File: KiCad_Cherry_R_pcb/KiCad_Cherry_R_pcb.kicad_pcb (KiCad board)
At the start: 2 copper layers, 188.7 x 100 mm, 89 parts, among them J1 AudioJack3_SwitchTR, SW1 7, SW10 I, SW11 O, SW12 P, SW13 [, SW14 ], SW15 H, SW16 J, SW17 K, SW18 L, SW19 ;, SW2 8, SW20 ', SW21 \, SW22 B, SW23 N, SW24 M, SW25 ,, SW26 ., SW27 /, SW28 Shift, SW29 Space, SW3 9, SW30 Conv, SW31 Win, SW32 Fn, SW33 ←, SW34 ↑, SW35 ↓, SW36 BS, SW37 Enter, SW38 Home, SW39 End, SW4 0, SW40 →, SW41 Free, SW42 PrtSc, SW5 -, SW6 =, SW7 `, SW8 Y, SW9 U, U1 Sparkfun_Pro_Micro

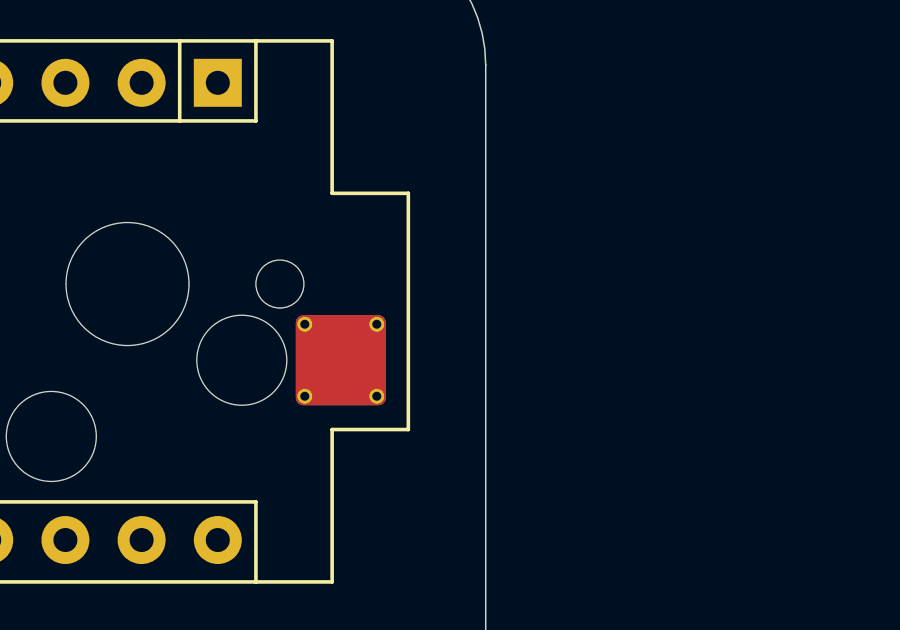
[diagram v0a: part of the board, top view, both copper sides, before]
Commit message: feat: Resetピンを追加
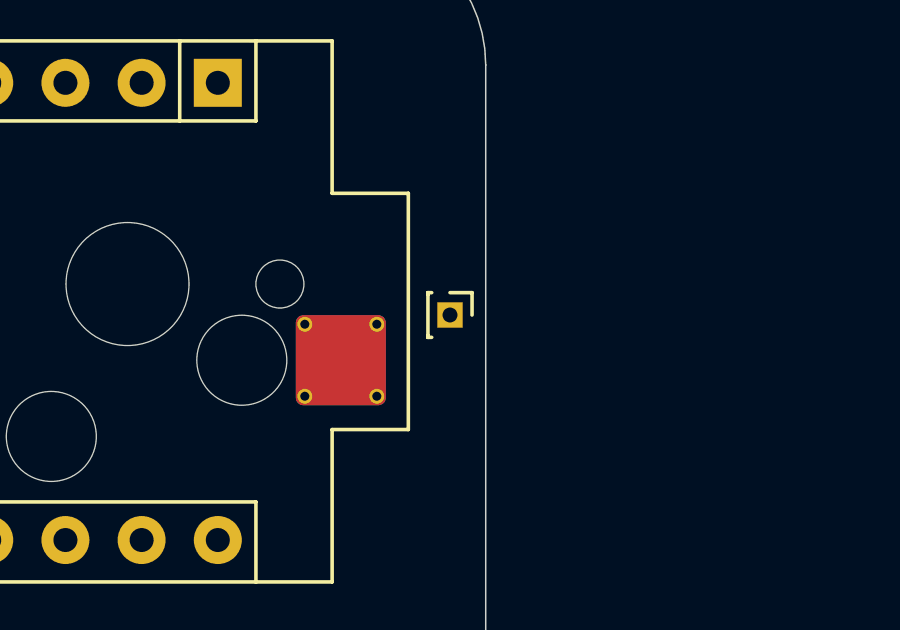
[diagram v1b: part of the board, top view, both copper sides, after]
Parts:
- added J2: Reset, Connector_PinHeader_1.00mm:PinHeader_1x01_P1.00mm_Vertical, F.Cu at (220.3, 48.8)
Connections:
- U1 pad 22: unconnected-(U1-RST-Pad22) -> Net-(J2-Pin_1)
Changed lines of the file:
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@@
 	(net 47 "Col5")
 	(net 48 "unconnected-(U1-RAW-Pad24)")
-	(net 49 "unconnected-(U1-RST-Pad22)")
+	(net 49 "Net-(J2-Pin_1)")
 	(net 50 "Net-(D33-A)")
 	(net 51 "unconnected-(U1-D0{slash}RX-Pad2)")
@@
 			(layers "*.Cu" "*.Mask")
 			(remove_unused_layers no)
-			(net 49 "unconnected-(U1-RST-Pad22)")
+			(net 49 "Net-(J2-Pin_1)")
 			(pinfunction "RST")
-			(pintype "input+no_connect")
+			(pintype "input")
 		)
 		(pad "23" thru_hole oval
@@
 			)
 			(scale
+				(xyz 1 1 1)
+			)
+			(rotate
+				(xyz 0 0 0)
+			)
+		)
+	)
+	(footprint "Connector_PinHeader_1.00mm:PinHeader_1x01_P1.00mm_Vertical"
+		(layer "F.Cu")
+		(at 220.26581 48.815666 -90)
+		(descr "Through hole straight pin header, 1x01, 1.00mm pitch, single row")
+		(tags "Through hole pin header THT 1x01 1.00mm single row")
+		(property "Reference" "J2"
+			(at 0 -1.61 90)
+			(layer "F.SilkS")
+			(hide yes)
+			(effects
+				(font
+					(size 1 1)
+					(thickness 0.15)
+				)
+			)
+		)
+		(property "Value" "Reset"
+			(at 0 1.61 90)
+			(layer "F.Fab")
+			(hide yes)
+			(effects
+				(font
+					(size 1 1)
+					(thickness 0.15)
+				)
+			)
+		)
+		(property "Datasheet" "~"
+			(at 0 0 90)
+			(layer "F.Fab")
+			(hide yes)
+			(effects
+				(font
+					(size 1.27 1.27)
+					(thickness 0.15)
+				)
+			)
+		)
+		(property "Description" "Generic connector, single row, 01x01, script generated"
+			(at 0 0 90)
+			(layer "F.Fab")
+			(hide yes)
+			(effects
+				(font
+					(size 1.27 1.27)
+					(thickness 0.15)
+				)
+			)
+		)
+		(property ki_fp_filters "Connector*:*_1x??_*")
+		(sheetname "/")
+		(sheetfile "KiCad_Cherry_R_pcb.kicad_sch")
+		(attr through_hole)
+		(fp_line
+			(start -0.745 0.735)
+			(end -0.685565 0.735)
+			(stroke
+				(width 0.12)
+				(type solid)
+			)
+			(layer "F.SilkS")
+		)
+		(fp_line
+			(start -0.745 0.735)
+			(end 0.745 0.735)
+			(stroke
+				(width 0.12)
+				(type solid)
+			)
+			(layer "F.SilkS")
+		)
+		(fp_line
+			(start -0.745 0.735)
+			(end -0.745 0.61)
+			(stroke
+				(width 0.12)
+				(type solid)
+			)
+			(layer "F.SilkS")
+		)
+		(fp_line
+			(start 0.685565 0.735)
+			(end 0.745 0.735)
+			(stroke
+				(width 0.12)
+				(type solid)
+			)
+			(layer "F.SilkS")
+		)
+		(fp_line
+			(start 0.745 0.735)
+			(end 0.745 0.61)
+			(stroke
+				(width 0.12)
+				(type solid)
+			)
+			(layer "F.SilkS")
+		)
+		(fp_line
+			(start -0.745 0)
+			(end -0.745 -0.735)
+			(stroke
+				(width 0.12)
+				(type solid)
+			)
+			(layer "F.SilkS")
+		)
+		(fp_line
+			(start -0.745 -0.735)
+			(end 0 -0.735)
+			(stroke
+				(width 0.12)
+				(type solid)
+			)
+			(layer "F.SilkS")
+		)
+		(fp_rect
+			(start -1.14 -1)
+			(end 1.14 1)
+			(stroke
+				(width 0.05)
+				(type solid)
+			)
+			(fill no)
+			(layer "F.CrtYd")
+		)
+		(fp_line
+			(start -0.635 0.5)
+			(end -0.635 -0.1825)
+			(stroke
+				(width 0.1)
+				(type solid)
+			)
+			(layer "F.Fab")
+		)
+		(fp_line
+			(start 0.635 0.5)
+			(end -0.635 0.5)
+			(stroke
+				(width 0.1)
+				(type solid)
+			)
+			(layer "F.Fab")
+		)
+		(fp_line
+			(start -0.635 -0.1825)
+			(end -0.3175 -0.5)
+			(stroke
+				(width 0.1)
+				(type solid)
+			)
+			(layer "F.Fab")
+		)
+		(fp_line
+			(start -0.3175 -0.5)
+			(end 0.635 -0.5)
+			(stroke
+				(width 0.1)
+				(type solid)
+			)
+			(layer "F.Fab")
+		)
+		(fp_line
+			(start 0.635 -0.5)
+			(end 0.635 0.5)
+			(stroke
+				(width 0.1)
+				(type solid)
+			)
+			(layer "F.Fab")
+		)
+		(fp_text user "${REFERENCE}"
+			(at 0 0 0)
+			(layer "F.Fab")
+			(effects
+				(font
+					(size 0.76 0.76)
+					(thickness 0.114)
+				)
+			)
+		)
+		(pad "1" thru_hole rect
+			(at 0 0 270)
+			(size 0.85 0.85)
+			(drill 0.5)
+			(layers "*.Cu" "*.Mask")
+			(remove_unused_layers no)
+			(net 49 "Net-(J2-Pin_1)")
+			(pinfunction "Pin_1")
+			(pintype "passive")
+		)
+		(embedded_fonts no)
+		(model "${KICAD9_3DMODEL_DIR}/Connector_PinHeader_1.00mm.3dshapes/PinHeader_1x01_P1.00mm_Vertical.step"
+			(offset
+				(xyz 0 0 0)
+			)
+			(scale

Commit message: feat: Rightのガワを用意
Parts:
- added D44: LED, LED_SMD:LED_0805_2012Metric, B.Cu at (35.4, 71.4)
- added R1: 10k, Resistor_SMD:R_0805_2012Metric, B.Cu at (35.4, 74.4)
- added REF**: MountingHole_2.2mm_M2, MountingHole:MountingHole_2.2mm_M2, F.Cu at (35.7, 45.2)
- added REF**: MountingHole_2.2mm_M2, MountingHole:MountingHole_2.2mm_M2, F.Cu at (152.4, 133.3)
- added REF**: MountingHole_2.2mm_M2, MountingHole:MountingHole_2.2mm_M2, F.Cu at (35.7, 85.7)
- added REF**: MountingHole_2.2mm_M2, MountingHole:MountingHole_2.2mm_M2, F.Cu at (104.8, 38.1)
- added REF**: MountingHole_2.2mm_M2, MountingHole:MountingHole_2.2mm_M2, F.Cu at (200.0, 133.3)
- added REF**: MountingHole_2.2mm_M2, MountingHole:MountingHole_2.2mm_M2, F.Cu at (200.0, 38.1)
- added REF**: MountingHole_2.2mm_M2, MountingHole:MountingHole_2.2mm_M2, F.Cu at (219.1, 85.7)
- added REF**: MountingHole_2.2mm_M2, MountingHole:MountingHole_2.2mm_M2, F.Cu at (219.1, 42.9)
- added REF**: MountingHole_2.2mm_M2, MountingHole:MountingHole_2.2mm_M2, F.Cu at (57.1, 38.1)
- added REF**: MountingHole_2.2mm_M2, MountingHole:MountingHole_2.2mm_M2, F.Cu at (35.7, 126.2)
- added REF**: MountingHole_2.2mm_M2, MountingHole:MountingHole_2.2mm_M2, F.Cu at (54.8, 133.3)
- added REF**: MountingHole_2.2mm_M2, MountingHole:MountingHole_2.2mm_M2, F.Cu at (219.1, 126.2)
- added REF**: MountingHole_2.2mm_M2, MountingHole:MountingHole_2.2mm_M2, F.Cu at (152.4, 38.1)
- added REF**: MountingHole_2.2mm_M2, MountingHole:MountingHole_2.2mm_M2, F.Cu at (104.8, 133.3)
- C1, C2, D1, D10, D11, D12, D13, D14, D15, D16, D17, D18, D19, D2, D20, D21, D22, D23, D24, D25, D26, D27, D28, D29, D3, D30, D32, D33, D34, D35, D37, D38, D39, D4, D40, D41, D42, D43, D5, D6, D7, D8, D9, J1, U1: moved to B.Cu
- moved J1 203.2 mm to (38.2, 94.7)
- moved D32 113.6 mm to (74.5, 139.0), turned to 180 degrees
- moved D33 113.6 mm to (74.5, 141.9), turned to 180 degrees
- moved D1 61.5 mm to (162.1, 145.4), turned to 180 degrees
- moved D2 61.5 mm to (162.1, 148.3), turned to 180 degrees
- moved D3 61.5 mm to (162.1, 151.3), turned to 180 degrees
- moved D4 61.5 mm to (162.1, 154.2), turned to 180 degrees
- moved D5 61.5 mm to (162.1, 157.2), turned to 180 degrees
- moved D6 61.5 mm to (162.1, 160.1), turned to 180 degrees
- moved D7 61.5 mm to (162.1, 163.1), turned to 180 degrees
- moved D10 52.9 mm to (157.8, 154.2), turned to 180 degrees
- moved D11 52.9 mm to (157.8, 157.2), turned to 180 degrees
- moved D12 52.9 mm to (157.8, 160.1), turned to 180 degrees
- moved D13 52.9 mm to (157.8, 163.1), turned to 180 degrees
- moved D37 52.9 mm to (157.8, 145.4), turned to 180 degrees
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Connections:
- U1 pad 2: unconnected-(U1-D0/RX-Pad2) -> Net-(D44-A)

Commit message: feat: ガワがすべて完成
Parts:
- added REF**: MountingHole_2.2mm_M2, MountingHole:MountingHole_2.2mm_M2, F.Cu at (35.1, 69.1)
- added REF**: MountingHole_2.2mm_M2, MountingHole:MountingHole_2.2mm_M2, F.Cu at (219.1, 59.5)
- added REF**: MountingHole_2.2mm_M2, MountingHole:MountingHole_2.2mm_M2, F.Cu at (35.1, 85.7)
- moved REF** 38.9 mm to (-2.98, 89.3)
- moved J1 17.4 mm to (38.1, 77.3)
- moved D44 10.7 mm to (35.1, 60.7)
- moved R1 10.1 mm to (35.1, 64.3)
- moved REF** 9.53 mm to (219.1, 95.2)
- moved REF** 3.62 mm to (35.1, 41.7)
- moved REF** 2.45 mm to (35.1, 123.8)
- moved REF** 2.38 mm to (219.1, 123.8)
- moved REF** 1.19 mm to (219.1, 41.7)
- turned SW15 to 180 degrees
- turned SW16 to 180 degrees
- turned SW17 to 180 degrees
- turned SW18 to 180 degrees
- turned SW19 to 180 degrees
- turned SW20 to 180 degrees
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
